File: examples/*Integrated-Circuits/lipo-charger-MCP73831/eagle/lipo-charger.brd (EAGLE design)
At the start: 0 parts

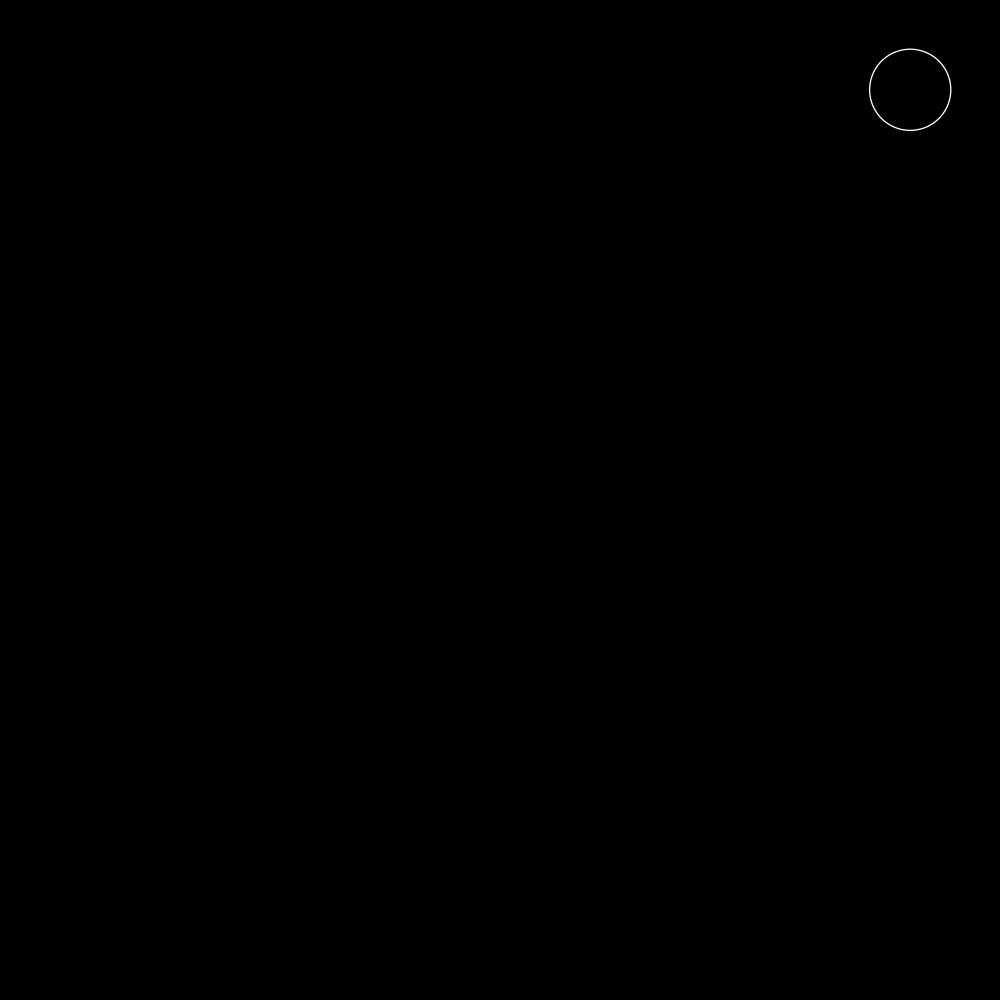
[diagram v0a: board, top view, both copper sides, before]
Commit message: marquee template; schematic images
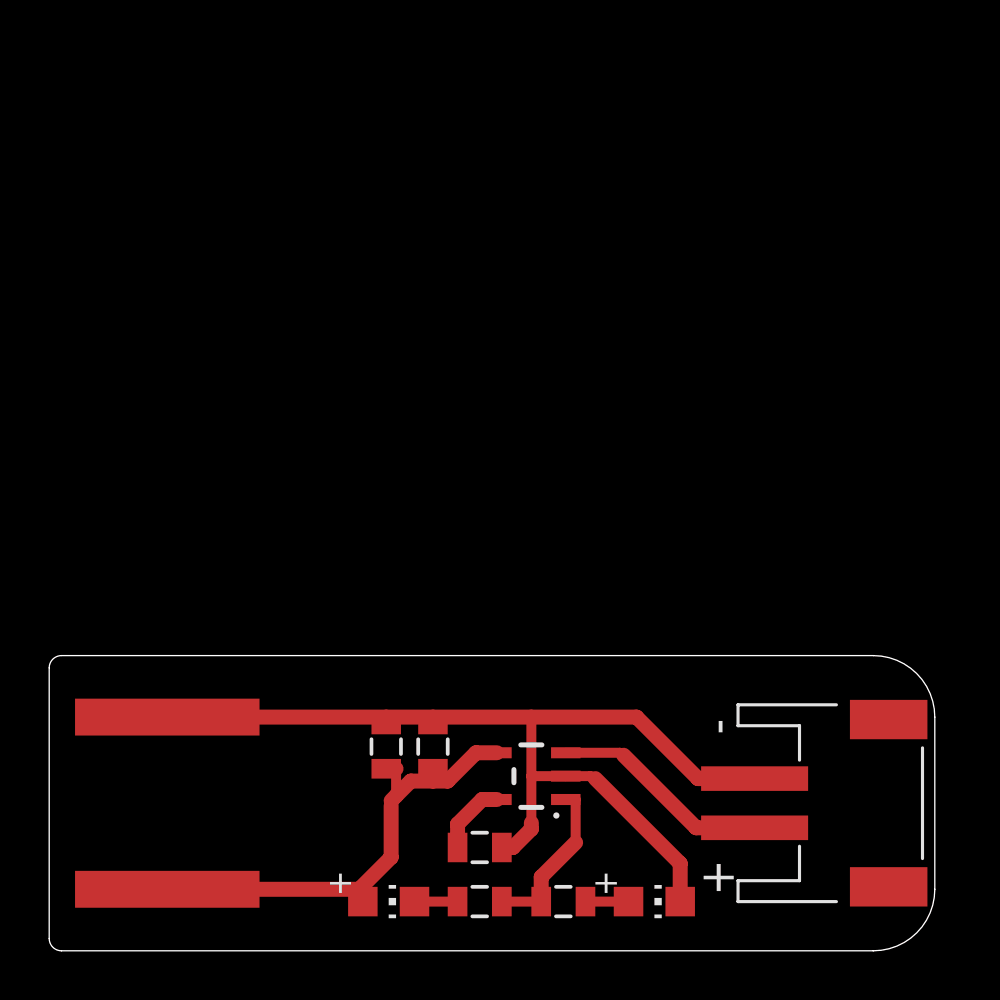
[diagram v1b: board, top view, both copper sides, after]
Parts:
- added C1: 10uF, homemade-hardware:0805
- added C2: 0.1uF, homemade-hardware:0805
- added IC1: IC_LIPO_CHARGER, homemade-hardware:SOT23-5
- added LED1: Red, homemade-hardware:CHIP-LED0805
- added LED2: Blue, homemade-hardware:CHIP-LED0805
- added R1, R2: 1k, homemade-hardware:0805
- added R3: 10k, homemade-hardware:0805
- added U$1: CONN_BATTERY-LIPO-HORIZ, homemade-hardware:JST-PH-2-SMT-RA
- added U$2: CONN_USB_PCB_POWER, homemade-hardware:USB-PCB-POWER
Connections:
- new net 5V: C1.1, C2.1, IC1.4, LED1.A, U$2.5V
- new net BATTERY: IC1.3, U$1.1
- new net CURRENT-CONTROL: IC1.5, R3.2
- new net GND: C1.2, C2.2, IC1.2, LED2.C, R3.1, U$1.2, U$2.GND
- new net N$2: LED1.C, R1.2
- new net N$3: LED2.A, R2.1
- new net STATUS: IC1.1, R1.1, R2.2
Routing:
- net GND: track 0.00 -> 40.6 mm
- net 5V: track 0.00 -> 19.7 mm
- net BATTERY: track 0.00 -> 8.94 mm
- net STATUS: track 0.00 -> 6.73 mm
- net CURRENT-CONTROL: track 0.00 -> 2.96 mm
- net N$2: track 0.00 -> 1.75 mm
- net N$3: track 0.00 -> 1.75 mm
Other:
- board outline added: 36 x 12 mm
- board text removed: "Max Size (70mm x 70mm)"
- board text removed: "Mounting Hole (3.3mm) place anywhere you want"
- board text removed: "The BRD and SCH file must have the same name or they will lose their link"
